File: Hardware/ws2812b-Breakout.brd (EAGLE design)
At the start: 17.8 x 12.7 mm, 11 parts

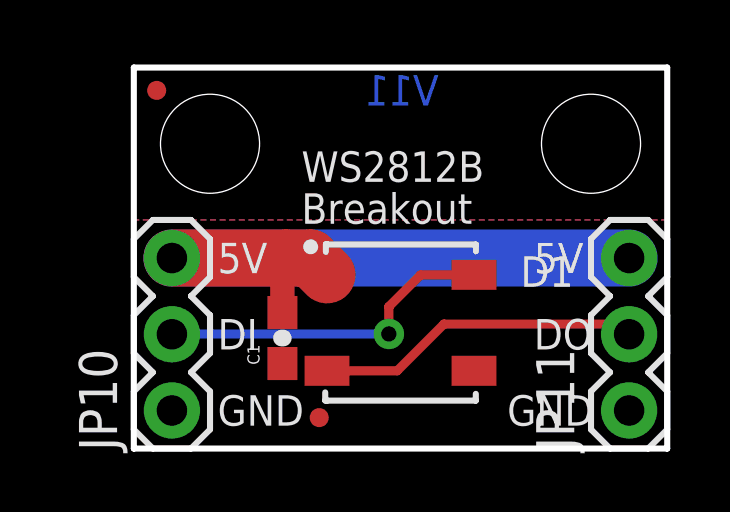
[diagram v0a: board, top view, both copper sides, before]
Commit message: Updated Frame / LED package.
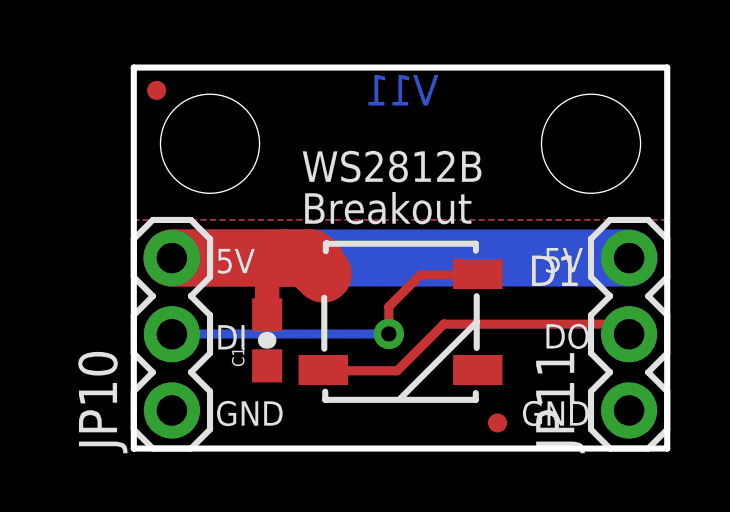
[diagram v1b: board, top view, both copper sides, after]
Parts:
- D1: value (none) -> WS2812B
- FRAME1: value FRAME-LETTER -> (none)
- moved FID2 5.95 mm to (12.1, 0.85)
- moved C1 0.51 mm to (4.45, 3.61)
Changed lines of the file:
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@@
 <layer number="45" name="Holes" color="7" fill="1" visible="yes" active="yes"/>
 <layer number="46" name="Milling" color="3" fill="1" visible="no" active="yes"/>
-<layer number="47" name="Measures" color="7" fill="1" visible="yes" active="yes"/>
+<layer number="47" name="Measures" color="7" fill="1" visible="no" active="yes"/>
 <layer number="48" name="Document" color="7" fill="1" visible="no" active="yes"/>
 <layer number="49" name="Reference" color="7" fill="1" visible="no" active="yes"/>
@@
 <layer number="56" name="wert" color="7" fill="1" visible="no" active="yes"/>
 <layer number="57" name="tCAD" color="7" fill="1" visible="no" active="no"/>
+<layer number="90" name="Modules" color="5" fill="1" visible="no" active="yes"/>
 <layer number="91" name="Nets" color="2" fill="1" visible="no" active="no"/>
 <layer number="92" name="Busses" color="1" fill="1" visible="no" active="no"/>
@@
 <layer number="111" name="LPC17xx" color="7" fill="1" visible="no" active="yes"/>
 <layer number="112" name="tSilk" color="7" fill="1" visible="no" active="yes"/>
+<layer number="113" name="IDFDebug" color="4" fill="1" visible="no" active="yes"/>
 <layer number="116" name="Patch_BOT" color="9" fill="4" visible="no" active="yes"/>
 <layer number="121" name="_tsilk" color="7" fill="1" visible="no" active="yes"/>
@@
 <wire x1="17.78" y1="12.7" x2="17.78" y2="0" width="0.2032" layer="20"/>
 <wire x1="17.78" y1="0" x2="0" y2="0" width="0.2032" layer="20"/>
-<text x="13.335" y="5.842" size="1.016" layer="21" font="vector" ratio="15">5V</text>
-<text x="2.794" y="3.302" size="1.016" layer="21" font="vector" ratio="15">DI</text>
-<text x="12.446" y="0.762" size="1.016" layer="21" font="vector" ratio="15">GND</text>
-<text x="2.794" y="5.842" size="1.016" layer="21" font="vector" ratio="15">5V</text>
-<text x="13.335" y="3.302" size="1.016" layer="21" font="vector" ratio="15">DO</text>
-<text x="2.794" y="0.762" size="1.016" layer="21" font="vector" ratio="15">GND</text>
+<text x="13.6525" y="5.872478125" size="0.8128" layer="21" font="vector" ratio="15">5V</text>
+<text x="2.7178" y="3.302" size="0.8128" layer="21" font="vector" ratio="15">DI</text>
+<text x="12.913359375" y="0.762" size="0.8128" layer="21" font="vector" ratio="15">GND</text>
+<text x="2.7178" y="5.842" size="0.8128" layer="21" font="vector" ratio="15">5V</text>
+<text x="13.655040625" y="3.332478125" size="0.8128" layer="21" font="vector" ratio="15">DO</text>
+<text x="2.7178" y="0.762" size="0.8128" layer="21" font="vector" ratio="15">GND</text>
 <text x="10.16" y="11.43" size="1.016" layer="16" ratio="20" rot="MR0">V11</text>
-<text x="4.572" y="5.842" size="1.016" layer="22" font="vector" ratio="15" rot="MR0">5V</text>
-<text x="14.986" y="3.302" size="1.016" layer="22" font="vector" ratio="15" rot="MR0">DO</text>
-<text x="5.334" y="0.762" size="1.016" layer="22" font="vector" ratio="15" rot="MR0">GND</text>
-<text x="14.986" y="5.842" size="1.016" layer="22" font="vector" ratio="15" rot="MR0">5V</text>
-<text x="4.318" y="3.302" size="1.016" layer="22" font="vector" ratio="15" rot="MR0">DI</text>
-<text x="14.986" y="0.762" size="1.016" layer="22" font="vector" ratio="15" rot="MR0">GND</text>
+<text x="4.04621875" y="5.839459375" size="0.8128" layer="22" font="vector" ratio="15" rot="MR0">5V</text>
+<text x="14.986" y="3.302" size="0.8128" layer="22" font="vector" ratio="15" rot="MR0">DO</text>
+<text x="4.79551875" y="0.7493" size="0.8128" layer="22" font="vector" ratio="15" rot="MR0">GND</text>
+<text x="14.986" y="5.8674" size="0.8128" layer="22" font="vector" ratio="15" rot="MR0">5V</text>
+<text x="3.812540625" y="3.317240625" size="0.8128" layer="22" font="vector" ratio="15" rot="MR0">DI</text>
+<text x="14.986" y="0.762" size="0.8128" layer="22" font="vector" ratio="15" rot="MR0">GND</text>
 <text x="5.588" y="8.89" size="1.016" layer="21" font="vector" ratio="15">WS2812B</text>
 <text x="5.588" y="7.493" size="1.016" layer="21" font="vector" ratio="15">Breakout</text>
@@
 </autorouter>
 <elements>
-<element name="C1" library="SparkFun-Capacitors" package="0603-CAP" value="0.1uF" x="4.953" y="3.683" rot="R90">
-<attribute name="PROD_ID" value="CAP-00810" x="4.953" y="3.683" size="1.778" layer="27" rot="R90" display="off"/>
-<attribute name="VALUE" value="0.1uF" x="4.953" y="3.683" size="1.778" layer="27" rot="R90" display="off"/>
+<element name="C1" library="SparkFun-Capacitors" package="0603-CAP" value="0.1uF" x="4.445" y="3.6068" rot="R90">
+<attribute name="PROD_ID" value="CAP-00810" x="4.445" y="3.6068" size="1.778" layer="27" rot="R90" display="off"/>
+<attribute name="VALUE" value="0.1uF" x="4.445" y="3.6068" size="1.778" layer="27" rot="R90" display="off"/>
 </element>
 <element name="JP1" library="SparkFun" package="STAND-OFF" value="STAND-OFF" x="15.24" y="10.16"/>
@@
 <element name="LOGO1" library="SparkFun-Aesthetics" package="OSHW-LOGO-S" value="OSHW-LOGOS" x="8.976359375" y="9.136378125" rot="MR0"/>
 <element name="FID1" library="SparkFun-Aesthetics" package="MICRO-FIDUCIAL" value="FIDUCIALUFIDUCIAL" x="0.762" y="11.938"/>
-<element name="FID2" library="SparkFun-Aesthetics" package="MICRO-FIDUCIAL" value="FIDUCIALUFIDUCIAL" x="6.179821875" y="1.031240625"/>
-<element name="FRAME1" library="SparkFun-Aesthetics" package="CREATIVE_COMMONS" value="FRAME-LETTER" x="-21.4515875" y="-12.7"/>
-<element name="D1" library="SparkFun-LED" package="WS2812B" value="" x="8.89" y="4.191"/>
+<element name="FID2" library="SparkFun-Aesthetics" package="MICRO-FIDUCIAL" value="FIDUCIALUFIDUCIAL" x="12.123421875" y="0.853440625"/>
+<element name="FRAME1" library="SparkFun-Aesthetics" package="CREATIVE_COMMONS" value="" x="-21.4515875" y="-12.7" smashed="yes">
+<attribute name="VERSION" value="v01" x="7.7584125" y="-2.54" size="1.27" layer="16" font="vector" ratio="15" rot="SMR0" display="off"/>
+<attribute name="DESIGNER" value="NAME" x="5.2184125" y="-12.7" size="1.778" layer="51" display="off"/>
+</element>
+<element name="D1" library="SparkFun-LED" package="WS2812B" value="WS2812B" x="8.89" y="4.2164"/>
 <element name="LOGO2" library="SparkFun-Aesthetics" package="SFE_LOGO_FLAME_.1" value="SFE_LOGO_FLAME.1_INCH" x="10.157459375" y="4.439921875" rot="MR0"/>
 </elements>
@@
 <wire x1="1.27" y1="6.35" x2="5.08" y2="6.35" width="1.905" layer="1"/>
 <wire x1="5.08" y1="6.35" x2="5.881" y2="6.35" width="1.905" layer="1"/>
-<wire x1="4.953" y1="4.533" x2="4.953" y2="6.223" width="0.8128" layer="1"/>
-<wire x1="4.953" y1="6.223" x2="5.08" y2="6.35" width="0.8128" layer="1"/>
-<wire x1="5.881" y1="6.35" x2="6.44" y2="5.791" width="1.905" layer="1"/>
+<wire x1="5.881" y1="6.35" x2="5.881" y2="6.223" width="1.905" layer="1"/>
+<wire x1="5.881" y1="6.223" x2="6.0588" y2="6.223" width="1.905" layer="1"/>
+<wire x1="4.572" y1="5.969" x2="4.699" y2="5.969" width="0.8128" layer="1"/>
+<wire x1="4.699" y1="5.969" x2="5.08" y2="6.35" width="0.8128" layer="1"/>
+<wire x1="6.0588" y1="6.223" x2="6.0588" y2="6.0706" width="1.905" layer="1"/>
+<wire x1="6.0588" y1="6.0706" x2="6.313" y2="5.8164" width="1.905" layer="1"/>
+<wire x1="4.445" y1="4.4568" x2="4.445" y2="5.715" width="0.8128" layer="1"/>
+<wire x1="4.445" y1="5.715" x2="4.699" y2="5.969" width="0.8128" layer="1"/>
 </signal>
 <signal name="GND">
 <contactref element="C1" pad="1"/>
-<polygon width="0.254" layer="1" isolate="0.3048">
+<polygon width="0.254" layer="1" spacing="0.889" isolate="0.3048">
 <vertex x="0" y="7.62"/>
 <vertex x="0" y="0"/>
@@
 <contactref element="JP11" pad="2"/>
 <contactref element="D1" pad="2"/>
-<wire x1="6.442340625" y1="2.593340625" x2="6.44" y2="2.591" width="0.3048" layer="1"/>
-<wire x1="6.44" y1="2.591" x2="8.778440625" y2="2.591" width="0.3048" layer="1"/>
 <wire x1="8.778440625" y1="2.591" x2="10.3378" y2="4.150359375" width="0.3048" layer="1"/>
 <wire x1="10.3378" y1="4.150359375" x2="16.169640625" y2="4.150359375" width="0.3048" layer="1"/>
 <wire x1="16.169640625" y1="4.150359375" x2="16.51" y2="3.81" width="0.3048" layer="1"/>
+<wire x1="8.778440625" y1="2.591" x2="6.3384" y2="2.591" width="0.3048" layer="1"/>
+<wire x1="6.3384" y1="2.591" x2="6.313" y2="2.6164" width="0.3048" layer="1"/>
 </signal>
 <signal name="DI">
@@
 <wire x1="8.50138125" y1="3.820159375" x2="8.50138125" y2="4.72948125" width="0.3048" layer="1"/>
 <wire x1="8.50138125" y1="4.72948125" x2="9.55801875" y2="5.78611875" width="0.3048" layer="1"/>
-<wire x1="9.55801875" y1="5.78611875" x2="11.33511875" y2="5.78611875" width="0.3048" layer="1"/>
-<wire x1="11.33511875" y1="5.78611875" x2="11.34" y2="5.791" width="0.3048" layer="1"/>
 <wire x1="1.27" y1="3.81" x2="1.280159375" y2="3.820159375" width="0.3048" layer="16"/>
 <wire x1="1.280159375" y1="3.820159375" x2="8.50138125" y2="3.820159375" width="0.3048" layer="16"/>
+<wire x1="9.55801875" y1="5.78611875" x2="11.43671875" y2="5.78611875" width="0.3048" layer="1"/>
+<wire x1="11.43671875" y1="5.78611875" x2="11.467" y2="5.8164" width="0.3048" layer="1"/>
 </signal>
 </signals>

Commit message: qc checklist items fixed
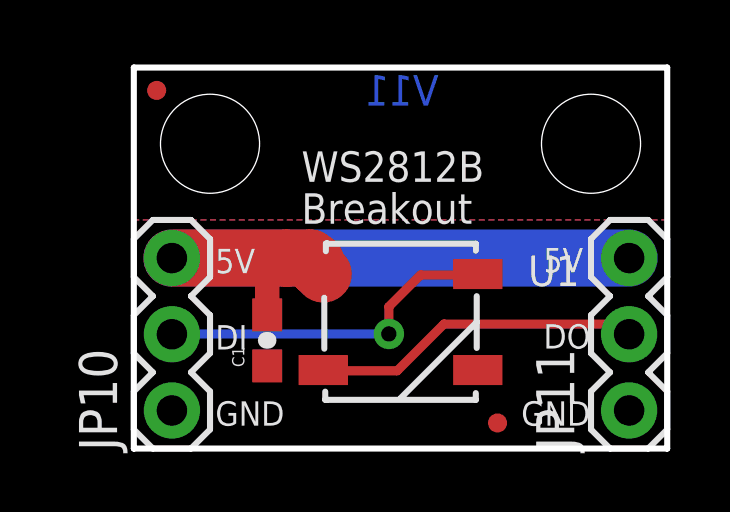
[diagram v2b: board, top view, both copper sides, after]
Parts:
- renumbered D1 to U1
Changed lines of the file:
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@@
 <?xml version="1.0" encoding="utf-8"?>
 <!DOCTYPE eagle SYSTEM "eagle.dtd">
-<eagle version="6.4">
+<eagle version="7.2.0">
 <drawing>
 <settings>
@@
 <layer number="45" name="Holes" color="7" fill="1" visible="yes" active="yes"/>
 <layer number="46" name="Milling" color="3" fill="1" visible="no" active="yes"/>
-<layer number="47" name="Measures" color="7" fill="1" visible="no" active="yes"/>
+<layer number="47" name="Measures" color="7" fill="1" visible="yes" active="yes"/>
 <layer number="48" name="Document" color="7" fill="1" visible="no" active="yes"/>
 <layer number="49" name="Reference" color="7" fill="1" visible="no" active="yes"/>
@@
 <layer number="56" name="wert" color="7" fill="1" visible="no" active="yes"/>
 <layer number="57" name="tCAD" color="7" fill="1" visible="no" active="no"/>
-<layer number="90" name="Modules" color="5" fill="1" visible="no" active="yes"/>
+<layer number="90" name="Modules" color="5" fill="1" visible="no" active="no"/>
 <layer number="91" name="Nets" color="2" fill="1" visible="no" active="no"/>
 <layer number="92" name="Busses" color="1" fill="1" visible="no" active="no"/>
@@
 <text x="8.89" y="-12.7" size="1.778" layer="51" font="vector" ratio="12">N. Seidle</text>
 <text x="-10.16" y="-15.24" size="1.778" layer="51" font="vector" ratio="12">Revised by: Patrick Alberts</text>
-<dimension x1="0" y1="17.78" x2="17.78" y2="17.78" x3="8.89" y3="19.05" textsize="1.778" textratio="15" layer="47"/>
-<dimension x1="-6.35" y1="0" x2="-6.35" y2="12.7" x3="-7.62" y3="6.35" textsize="1.778" textratio="15" layer="47"/>
+<dimension x1="0" y1="17.78" x2="17.78" y2="17.78" x3="8.89" y3="19.05" textsize="1.778" textratio="15" layer="47" unit="inch"/>
+<dimension x1="-6.35" y1="0" x2="-6.35" y2="12.7" x3="-7.62" y3="6.35" textsize="1.778" textratio="15" layer="47" unit="inch"/>
 </plain>
 <attributes>
@@
 <pass name="Default">
 <param name="RoutingGrid" value="50mil"/>
+<param name="AutoGrid" value="1"/>
+<param name="Efforts" value="0"/>
+<param name="TopRouterVariant" value="1"/>
 <param name="tpViaShape" value="round"/>
 <param name="PrefDir.1" value="|"/>
@@
 <attribute name="DESIGNER" value="NAME" x="5.2184125" y="-12.7" size="1.778" layer="51" display="off"/>
 </element>
-<element name="D1" library="SparkFun-LED" package="WS2812B" value="WS2812B" x="8.89" y="4.2164"/>
+<element name="U1" library="SparkFun-LED" package="WS2812B" value="WS2812B" x="8.89" y="4.2164">
+<attribute name="PROD_ID" value="DIO-12503" x="8.89" y="4.2164" size="1.778" layer="27" display="off"/>
+</element>
 <element name="LOGO2" library="SparkFun-Aesthetics" package="SFE_LOGO_FLAME_.1" value="SFE_LOGO_FLAME.1_INCH" x="10.157459375" y="4.439921875" rot="MR0"/>
 </elements>
@@
 <contactref element="JP11" pad="3"/>
 <wire x1="16.51" y1="6.35" x2="1.27" y2="6.35" width="1.905" layer="16"/>
-<contactref element="D1" pad="1"/>
+<contactref element="U1" pad="1"/>
 <wire x1="1.27" y1="6.35" x2="5.08" y2="6.35" width="1.905" layer="1"/>
 <wire x1="5.08" y1="6.35" x2="5.881" y2="6.35" width="1.905" layer="1"/>
@@
 <contactref element="JP10" pad="1"/>
 <contactref element="JP11" pad="1"/>
-<contactref element="D1" pad="3"/>
+<contactref element="U1" pad="3"/>
 </signal>
 <signal name="DO">
 <contactref element="JP11" pad="2"/>
-<contactref element="D1" pad="2"/>
+<contactref element="U1" pad="2"/>
 <wire x1="8.778440625" y1="2.591" x2="10.3378" y2="4.150359375" width="0.3048" layer="1"/>
 <wire x1="10.3378" y1="4.150359375" x2="16.169640625" y2="4.150359375" width="0.3048" layer="1"/>
@@
 <contactref element="JP10" pad="2"/>
 <via x="8.50138125" y="3.820159375" extent="1-16" drill="0.508"/>
-<contactref element="D1" pad="4"/>
+<contactref element="U1" pad="4"/>
 <wire x1="8.50138125" y1="3.820159375" x2="8.50138125" y2="4.72948125" width="0.3048" layer="1"/>
 <wire x1="8.50138125" y1="4.72948125" x2="9.55801875" y2="5.78611875" width="0.3048" layer="1"/>

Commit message: Fixed qc issues
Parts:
- removed JP10: INPUT, SparkFun-Connectors:1X03
- added JP15: STAND-OFF, SparkFun:STAND-OFF
- JP1: value STAND-OFF -> INPUT; device SparkFun:STAND-OFF -> SparkFun-Connectors:1X03
- moved JP1 16.6 mm to (1.27, 1.27), turned to 90 degrees
- renumbered JP11 to JP2
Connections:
- net DI: now also JP1.2; no longer JP10.2
- net GND: now also JP1.1; no longer JP10.1
- net VCC: now also JP1.3; no longer JP10.3
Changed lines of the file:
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@@
 <attribute name="VALUE" value="0.1uF" x="4.445" y="3.6068" size="1.778" layer="27" rot="R90" display="off"/>
 </element>
-<element name="JP1" library="SparkFun" package="STAND-OFF" value="STAND-OFF" x="15.24" y="10.16"/>
+<element name="JP15" library="SparkFun" package="STAND-OFF" value="STAND-OFF" x="15.24" y="10.16"/>
 <element name="JP4" library="SparkFun" package="STAND-OFF" value="STAND-OFF" x="2.54" y="10.16"/>
-<element name="JP10" library="SparkFun-Connectors" package="1X03" value="INPUT" x="1.27" y="1.27" rot="R90"/>
-<element name="JP11" library="SparkFun-Connectors" package="1X03" value="OUTPUT" x="16.51" y="1.27" rot="R90"/>
+<element name="JP1" library="SparkFun-Connectors" package="1X03" value="INPUT" x="1.27" y="1.27" rot="R90"/>
+<element name="JP2" library="SparkFun-Connectors" package="1X03" value="OUTPUT" x="16.51" y="1.27" rot="R90"/>
 <element name="LOGO1" library="SparkFun-Aesthetics" package="OSHW-LOGO-S" value="OSHW-LOGOS" x="8.976359375" y="9.136378125" rot="MR0"/>
 <element name="FID1" library="SparkFun-Aesthetics" package="MICRO-FIDUCIAL" value="FIDUCIALUFIDUCIAL" x="0.762" y="11.938"/>
@@
 <signal name="VCC">
 <contactref element="C1" pad="2"/>
-<contactref element="JP10" pad="3"/>
-<contactref element="JP11" pad="3"/>
+<contactref element="JP1" pad="3"/>
+<contactref element="JP2" pad="3"/>
 <wire x1="16.51" y1="6.35" x2="1.27" y2="6.35" width="1.905" layer="16"/>
 <contactref element="U1" pad="1"/>
@@
 <vertex x="17.78" y="7.62"/>
 </polygon>
-<contactref element="JP10" pad="1"/>
-<contactref element="JP11" pad="1"/>
+<contactref element="JP1" pad="1"/>
+<contactref element="JP2" pad="1"/>
 <contactref element="U1" pad="3"/>
 </signal>
 <signal name="DO">
-<contactref element="JP11" pad="2"/>
+<contactref element="JP2" pad="2"/>
 <contactref element="U1" pad="2"/>
 <wire x1="8.778440625" y1="2.591" x2="10.3378" y2="4.150359375" width="0.3048" layer="1"/>
@@
 </signal>
 <signal name="DI">
-<contactref element="JP10" pad="2"/>
+<contactref element="JP1" pad="2"/>
 <via x="8.50138125" y="3.820159375" extent="1-16" drill="0.508"/>
 <contactref element="U1" pad="4"/>

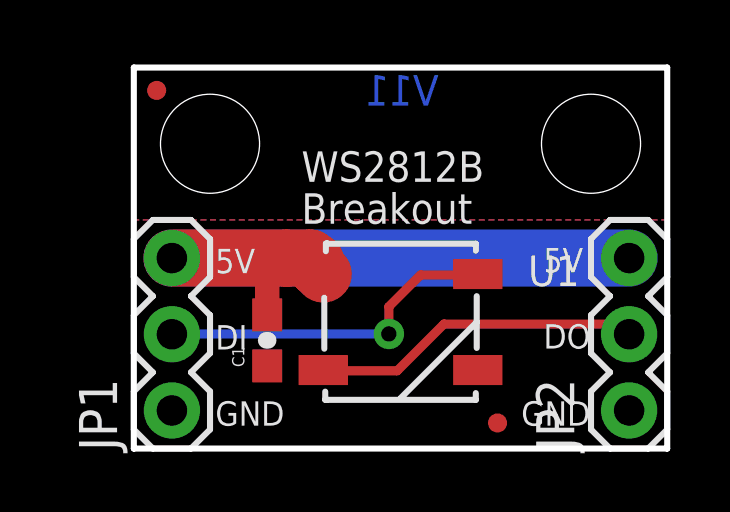
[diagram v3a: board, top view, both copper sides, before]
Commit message: changed fids to regular size
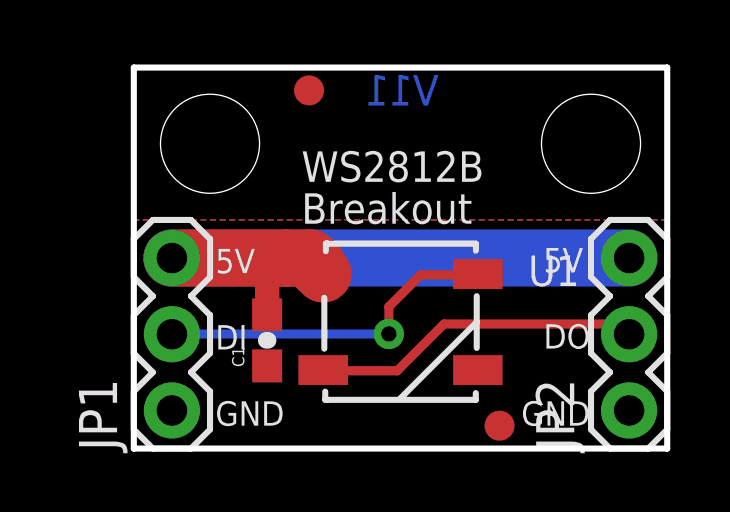
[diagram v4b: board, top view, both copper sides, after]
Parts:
- FID1, FID2: value FIDUCIALUFIDUCIAL -> FIDUCIAL1X2; device SparkFun-Aesthetics:MICRO-FIDUCIAL -> SparkFun-Aesthetics:FIDUCIAL-1X2
- moved FID1 5.08 mm to (5.84, 11.9)
- moved FID2 0.11 mm to (12.2, 0.76)
